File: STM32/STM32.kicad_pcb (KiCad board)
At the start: 2 copper layers, 30 x 45 mm, 7 parts, among them J1 Power_conn, P1 SWD_TC, U1 STM32F042K4, U2 LD1117S33TR, U3 STM32F042SHIELD

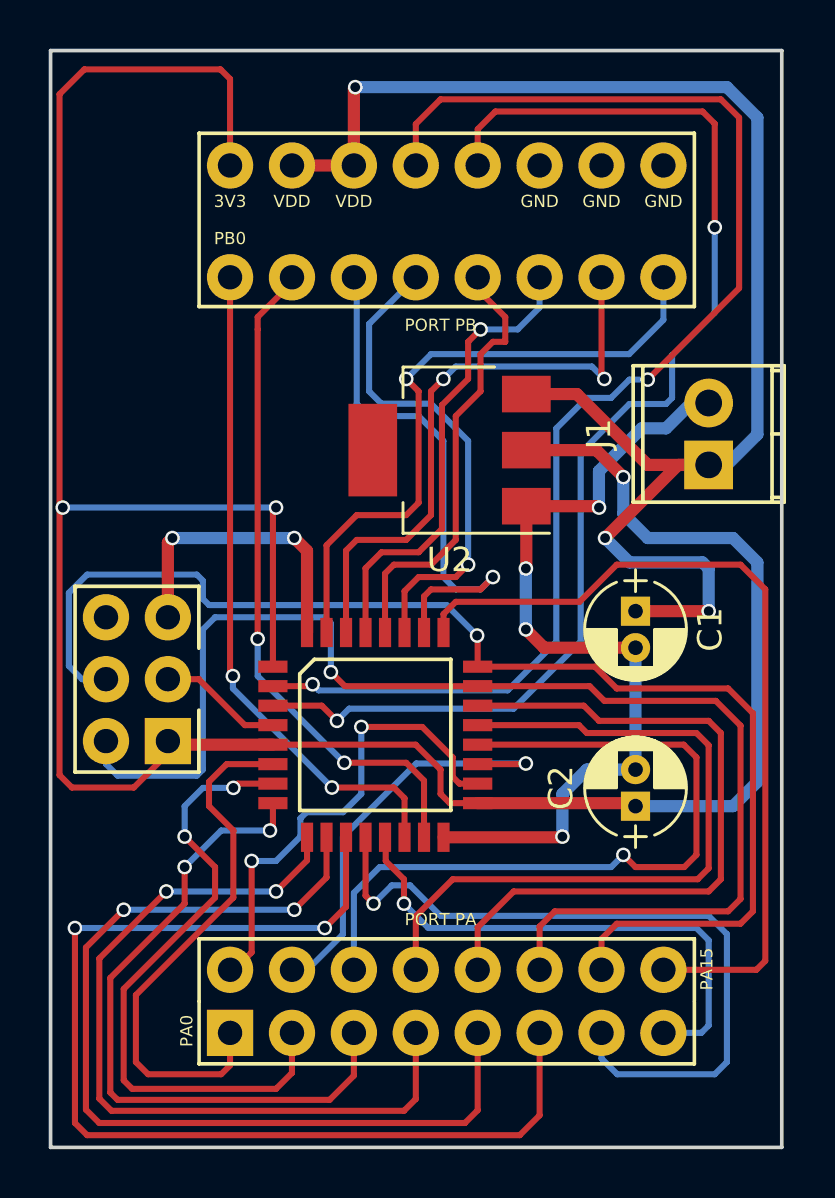
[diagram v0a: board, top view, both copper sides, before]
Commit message: added power conn
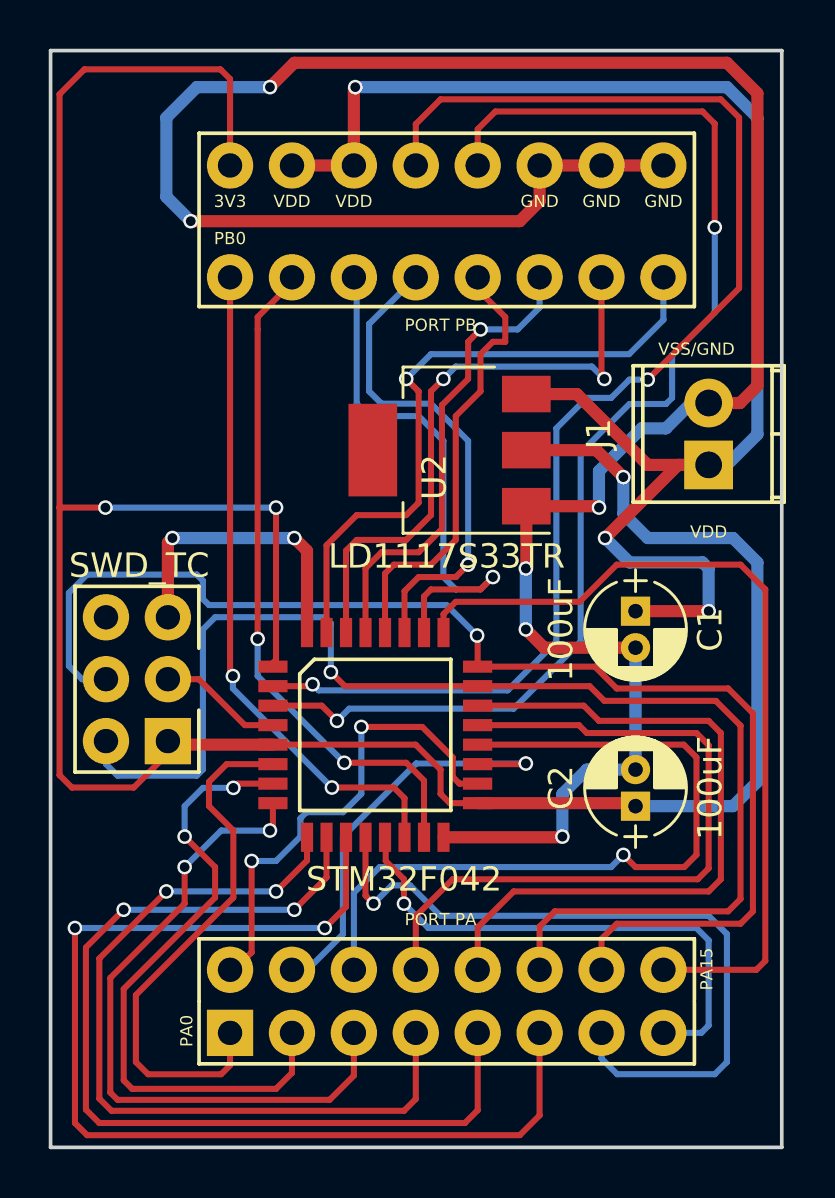
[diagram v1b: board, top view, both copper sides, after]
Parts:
- U1: value STM32F042K4 -> STM32F042
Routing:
- net /VSS: track 47.5 -> 113.4 mm, vias 6 -> 8
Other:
- board text added: "VDD"
- board text added: "VSS/GND"
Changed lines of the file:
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@@
   (general
     (links 48)
-    (no_connects 5)
+    (no_connects 0)
     (area 0 0 0 0)
     (thickness 1.6)
-    (drawings 4)
-    (tracks 422)
+    (drawings 6)
+    (tracks 441)
     (zones 0)
     (modules 7)
@@
   (page A4)
   (layers
-    (0 F.Cu signal)
-    (31 B.Cu signal)
+    (0 F.Cu signal hide)
+    (31 B.Cu signal hide)
     (32 B.Adhes user hide)
     (33 F.Adhes user hide)
@@
   )
   (setup
-    (last_trace_width 0.5)
+    (last_trace_width 0.25)
     (user_trace_width 0.5)
     (user_trace_width 0.75)
@@
     (pad_to_mask_clearance 0.2)
     (aux_axis_origin 0 0)
-    (visible_elements FFFFFF7F)
+    (visible_elements FFFFF77F)
     (pcbplotparams
       (layerselection 0x00030_80000001)
@@
       (effects (font (size 1 1) (thickness 0.15)))
     )
-    (fp_text value 100uF (at 0.75 3.06 270) (layer F.Fab)
+    (fp_text value 100uF (at 0.75 3.06 270) (layer F.SilkS)
       (effects (font (size 1 1) (thickness 0.15)))
     )
@@
       (effects (font (size 1 1) (thickness 0.15)))
     )
-    (fp_text value SWD_TC (at 4.664 0.092 180) (layer F.Fab)
+    (fp_text value SWD_TC (at 4.664 0.092 180) (layer F.SilkS)
       (effects (font (size 1 1) (thickness 0.15)))
     )
@@
       (effects (font (size 1 1) (thickness 0.15)))
     )
-    (fp_text value STM32F042K4 (at 0 5.75) (layer F.Fab)
+    (fp_text value STM32F042 (at 1.178 5.923) (layer F.SilkS)
       (effects (font (size 1 1) (thickness 0.15)))
     )
@@
       (effects (font (size 1 1) (thickness 0.15)))
     )
-    (fp_text value 100uF (at 0.75 3.06 90) (layer F.Fab)
+    (fp_text value 100uF (at 0.75 3.06 90) (layer F.SilkS)
       (effects (font (size 1 1) (thickness 0.15)))
     )
@@
     (tags "CMS SOT")
     (attr smd)
-    (fp_text reference U2 (at 0 -4.5 180) (layer F.SilkS)
+    (fp_text reference U2 (at 0.62 -1.107 270) (layer F.SilkS)
       (effects (font (size 1 1) (thickness 0.15)))
     )
-    (fp_text value LD1117S33TR (at 0 4.5 180) (layer F.Fab)
+    (fp_text value LD1117S33TR (at 0.12 -4.357 180) (layer F.SilkS)
       (effects (font (size 1 1) (thickness 0.15)))
     )
@@
       (rotate (xyz 0 0 90))
     )
+  )
+  (gr_text VSS/GND (at 176.5 92.25) (layer F.SilkS)
+    (effects (font (size 0.5 0.5) (thickness 0.125)))
+  )
+  (gr_text VDD (at 177 99.75) (layer F.SilkS)
+    (effects (font (size 0.5 0.5) (thickness 0.125)))
   )
   (gr_line (start 180 80) (end 180 125) (angle 90) (layer Edge.Cuts) (width 0.15))
@@
   (segment (start 174.5 97) (end 177 97) (width 0.5) (layer F.Cu) (net 1))
   (segment (start 171.593 94.093) (end 174.5 97) (width 0.5) (layer F.Cu) (net 1))
+  (segment (start 172.604 84.714) (end 175.144 84.714) (width 0.5) (layer F.Cu) (net 2))
+  (segment (start 170.064 84.714) (end 172.604 84.714) (width 0.5) (layer F.Cu) (net 2))
+  (segment (start 177 94.46) (end 178.29 94.46) (width 0.5) (layer F.Cu) (net 2))
+  (segment (start 170.064 86.186) (end 170.064 84.714) (width 0.5) (layer F.Cu) (net 2))
+  (segment (start 169.25 87) (end 170.064 86.186) (width 0.5) (layer F.Cu) (net 2))
+  (segment (start 155.75 87) (end 169.25 87) (width 0.5) (layer F.Cu) (net 2))
+  (via (at 155.75 87) (size 0.6) (drill 0.4) (layers F.Cu B.Cu) (net 2))
+  (segment (start 154.75 86) (end 155.75 87) (width 0.5) (layer B.Cu) (net 2))
+  (segment (start 154.75 82.75) (end 154.75 86) (width 0.5) (layer B.Cu) (net 2))
+  (segment (start 156 81.5) (end 154.75 82.75) (width 0.5) (layer B.Cu) (net 2))
+  (segment (start 159 81.5) (end 156 81.5) (width 0.5) (layer B.Cu) (net 2))
+  (via (at 159 81.5) (size 0.6) (drill 0.4) (layers F.Cu B.Cu) (net 2))
+  (segment (start 160 80.5) (end 159 81.5) (width 0.5) (layer F.Cu) (net 2))
+  (segment (start 177.75 80.5) (end 160 80.5) (width 0.5) (layer F.Cu) (net 2))
+  (segment (start 179 81.75) (end 177.75 80.5) (width 0.5) (layer F.Cu) (net 2))
+  (segment (start 179 93.75) (end 179 81.75) (width 0.5) (layer F.Cu) (net 2))
+  (segment (start 178.29 94.46) (end 179 93.75) (width 0.5) (layer F.Cu) (net 2))
   (segment (start 177 94.46) (end 176.29 94.46) (width 0.5) (layer B.Cu) (net 2))
   (segment (start 176.29 94.46) (end 175.25 95.5) (width 0.5) (layer B.Cu) (net 2))
@@
   (segment (start 157.969 107.677) (end 159.122 107.677) (width 0.25) (layer F.Cu) (net 29))
   (segment (start 156.083 105.791) (end 157.969 107.677) (width 0.25) (layer F.Cu) (net 29))
-  (segment (start 159.122 105.277) (end 159.122 98.878) (width 0.25) (layer F.Cu) (net 31))
-  (via (at 150.5 98.75) (size 0.6) (drill 0.4) (layers F.Cu B.Cu) (net 31))
-  (segment (start 159.25 98.75) (end 150.5 98.75) (width 0.25) (layer B.Cu) (net 31))
+  (segment (start 150.368 98.75) (end 152.25 98.75) (width 0.25) (layer F.Cu) (net 31))
+  (segment (start 159.25 105) (end 159.122 105.128) (width 0.25) (layer F.Cu) (net 31))
+  (segment (start 159.25 104.5) (end 159.25 105) (width 0.25) (layer F.Cu) (net 31))
+  (segment (start 159.25 98.75) (end 159.25 104.5) (width 0.25) (layer F.Cu) (net 31))
   (via (at 159.25 98.75) (size 0.6) (drill 0.4) (layers F.Cu B.Cu) (net 31))
-  (segment (start 159.122 98.878) (end 159.25 98.75) (width 0.25) (layer F.Cu) (net 31))
-  (segment (start 150.5 98.75) (end 150.368 98.75) (width 0.25) (layer F.Cu) (net 31))
-  (segment (start 150.368 98.75) (end 150.5 98.75) (width 0.25) (layer F.Cu) (net 31))
+  (segment (start 152.25 98.75) (end 159.25 98.75) (width 0.25) (layer B.Cu) (net 31))
+  (via (at 152.25 98.75) (size 0.6) (drill 0.4) (layers F.Cu B.Cu) (net 31))
+  (segment (start 159.122 105.128) (end 159.122 105.277) (width 0.25) (layer F.Cu) (net 31))
   (segment (start 159.122 108.477) (end 164.977 108.477) (width 0.25) (layer F.Cu) (net 31))
   (segment (start 166.377 110.877) (end 167.522 110.877) (width 0.25) (layer F.Cu) (net 31))
@@
   (segment (start 151.384 80.772) (end 156.972 80.772) (width 0.25) (layer F.Cu) (net 31))
   (segment (start 150.368 81.788) (end 151.384 80.772) (width 0.25) (layer F.Cu) (net 31))
-  (segment (start 150.368 109.728) (end 150.368 81.788) (width 0.25) (layer F.Cu) (net 31))
+  (segment (start 150.368 109.728) (end 150.368 98.75) (width 0.25) (layer F.Cu) (net 31))
+  (segment (start 150.368 98.75) (end 150.368 81.788) (width 0.25) (layer F.Cu) (net 31))
   (segment (start 150.876 110.236) (end 150.368 109.728) (width 0.25) (layer F.Cu) (net 31))
   (segment (start 153.416 110.236) (end 150.876 110.236) (width 0.25) (layer F.Cu) (net 31))
@@
     (connect_pads (clearance 0.508))
     (min_thickness 0.254)
-    (fill (arc_segments 16) (thermal_gap 0.508) (thermal_bridge_width 0.508))
+    (fill yes (arc_segments 16) (thermal_gap 0.508) (thermal_bridge_width 0.508))
     (polygon
       (pts
@@
     (connect_pads (clearance 0.508))
     (min_thickness 0.254)
-    (fill (arc_segments 16) (thermal_gap 0.508) (thermal_bridge_width 0.508))
+    (fill yes (arc_segments 16) (thermal_gap 0.508) (thermal_bridge_width 0.508))
     (polygon
       (pts

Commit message: finished protoying board
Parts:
- added ?: , Symbols:Symbol_Danger_CopperTop_Small, B.Cu at (155.4, 94.2)
- added G***: LOGO, footprints:LOGO, F.Cu at (156.0, 92.4)
- added REF***: WEEE-Logo_4.2x6mm_SilkScreen, Symbols:WEEE-Logo_4.2x6mm_SilkScreen, F.Cu at (153.4, 83.8)
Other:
- board text added: "STM32F042 PROTOTYPING BOARD MARCH 2017"
